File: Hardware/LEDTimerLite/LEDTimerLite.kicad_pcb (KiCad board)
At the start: 4 copper layers, 37.3 x 23.1 mm, 27 parts, among them J1 Program, J2 LED, J3 PWR, Q1 S8050, SW1 SW_Push, SW4 SW_PWR, U1 AP7383-36WW7, U2 PIC16LF18326, U4 BCR_421U_E6327, Y1 32.768 kHz

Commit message: LTL: try new PCB layout
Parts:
- added D2: Red LED, LED_SMD:LED_0805_2012Metric_Pad1.15x1.40mm_HandSolder, F.Cu at (138.8, 64.8)
- added R4: 560, Resistor_SMD:R_0805_2012Metric_Pad1.20x1.40mm_HandSolder, F.Cu at (134.0, 69.8)
- C1, C2, D1, Q1, R1, R2, R3, R5, U1, U4: moved to F.Cu
- J2, J3: moved to B.Cu
- moved H1 51.0 mm to (93.1, 70.4)
- moved H4 31.1 mm to (137.5, 70.4)
- moved J1 30.8 mm to (122.1, 58.3)
- moved H3 29.4 mm to (137.5, 59.2)
- moved J3 27.6 mm to (101.1, 63.5)
- moved R3 26.7 mm to (108.7, 69.5), turned to 90 degrees
- moved SW4 26.2 mm to (100.0, 70.5)
- moved C1 25.1 mm to (99.2, 64.8), turned to 90 degrees
- moved U1 25.1 mm to (96.0, 64.8)
- moved D1 22.1 mm to (104.4, 64.4), turned to 180 degrees
- moved H2 21.8 mm to (93.1, 59.2)
- moved Q1 21.5 mm to (105.1, 61.0)
- moved R1 20.7 mm to (101.1, 61.3)
- moved R2 20.7 mm to (101.1, 59.3)
- moved CG1 19.4 mm to (118.6, 63.0), turned to 90 degrees
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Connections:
- U2 pad 8: unconnected-(U2-RC1-Pad8) -> /LED
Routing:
- net /LED_EN_PWM: track 24.5 -> 0.00 mm, vias 3 -> 0
- net +5V: track 24.5 -> 0.00 mm
- net Net-(U2-RC0): track 18.3 -> 0.00 mm
- net /~{MCLR}/VPP: track 17.6 -> 0.00 mm, vias 1 -> 0
- net /ICSPCLK_RXD: track 15.5 -> 0.00 mm, vias 1 -> 0
- net Net-(U1-VOUT): track 13.3 -> 0.00 mm, vias 2 -> 0
- net /ICSPDAT_TXD: track 12.9 -> 0.00 mm, vias 1 -> 0
- net Net-(U4-Rext): track 12.1 -> 0.00 mm, vias 1 -> 0
- net /LDO_SENSE: track 10.4 -> 0.00 mm, vias 1 -> 0
- net Net-(SW4-C): track 10.2 -> 0.00 mm
- net Net-(J2-Pin_2): track 8.03 -> 0.00 mm
- net Net-(U2-RA5): track 6.34 -> 0.00 mm
- net Net-(CD1-Pad1): track 4.94 -> 0.00 mm
- net Net-(Q1-B): track 4.82 -> 0.00 mm
- net Net-(U2-RA4): track 4.55 -> 0.00 mm
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- removed copper zone on In2.Cu, net +3V3
- removed copper zone on In1.Cu, net GND
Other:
- board size 37.3 x 23.1 mm -> 49.5 x 16.3 mm

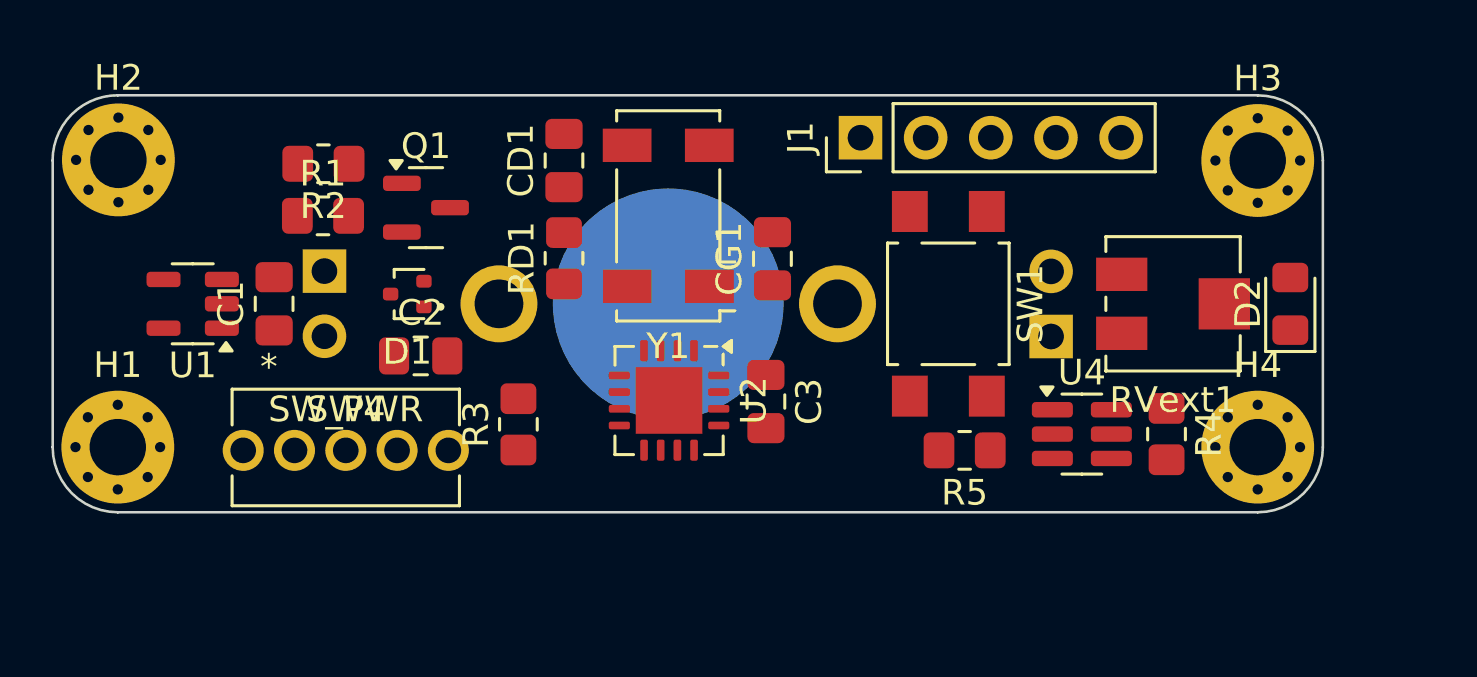
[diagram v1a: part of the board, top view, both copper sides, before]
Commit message: LTL: improve track routing
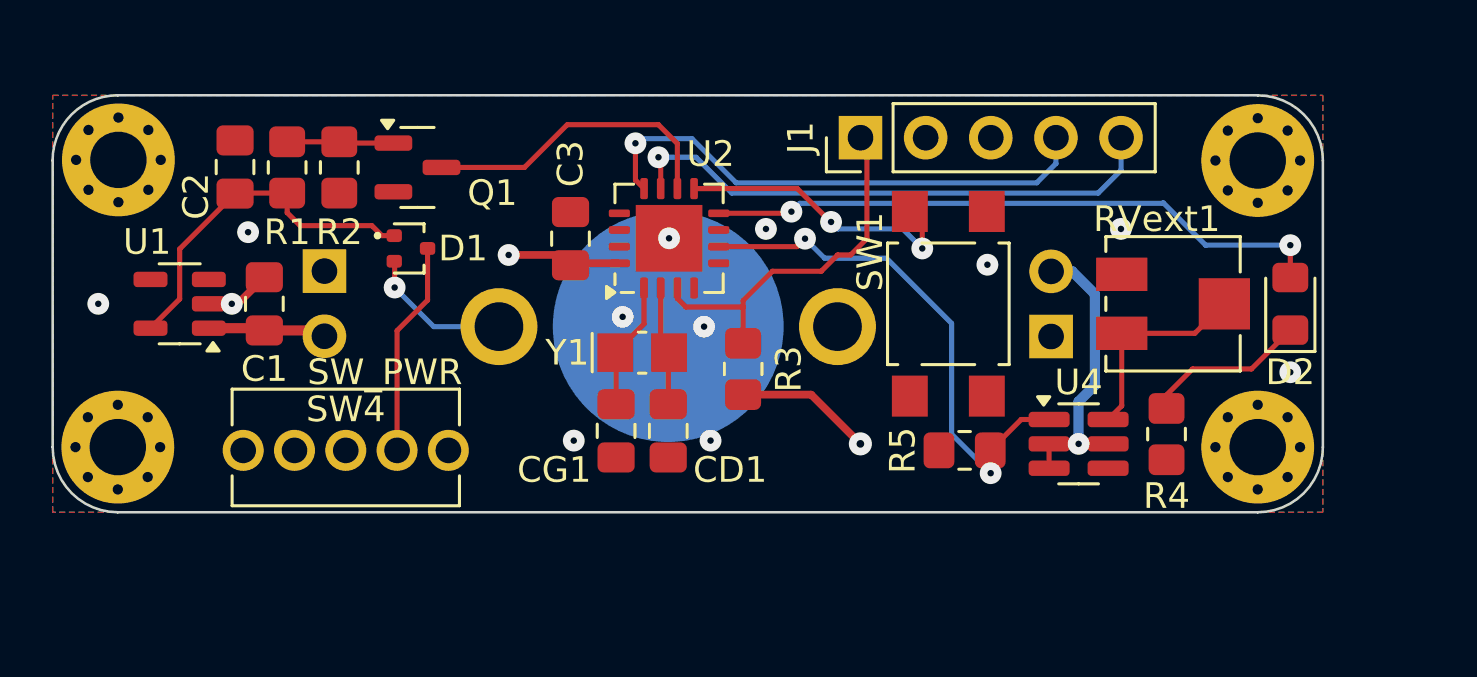
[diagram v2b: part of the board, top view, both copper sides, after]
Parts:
- removed RD1: 220k, Resistor_SMD:R_0805_2012Metric_Pad1.20x1.40mm_HandSolder
- Y1: footprint Crystal:Crystal_SMD_Abracon_ABS25-4Pin_8.0x3.8mm -> Crystal:Crystal_SMD_MicroCrystal_CC8V-T1A-2Pin_2.0x1.2mm_HandSoldering
- moved CD1 11.3 mm to (114.6, 69.7), turned to -90 degrees
- moved C2 10.3 mm to (97.7, 59.4), turned to 90 degrees
- moved C3 9.92 mm to (110.7, 62.2), turned to 90 degrees
- moved CG1 9.07 mm to (112.5, 69.7), turned to -90 degrees
- moved R3 9.03 mm to (117.5, 67.3)
- moved U2 6.32 mm to (114.6, 62.2), turned to 90 degrees
- moved Y1 5.43 mm to (113.5, 66.7), turned to 0 degrees
- moved R1 2.35 mm to (99.7, 59.5), turned to 90 degrees
- moved D1 1.78 mm to (104.5, 62.6), turned to 0 degrees
- moved Q1 1.60 mm to (104.8, 59.5)
- moved BT1 0.89 mm to (114.6, 65.7)
- moved R2 0.64 mm to (101.7, 59.5), turned to -90 degrees
- moved U1 0.51 mm to (95.5, 64.8)
- moved U4 0.40 mm to (130.6, 70.2)
- moved C1 0.38 mm to (98.8, 64.8)
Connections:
- CD1 pad 1: Net-(CD1-Pad1) -> Net-(U2-RA4)
- Y1 pad 2: GND -> Net-(U2-RA4)
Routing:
- net +5V: track 0.00 -> 35.6 mm
- net /LED: track 0.00 -> 24.4 mm, vias 0 -> 2
- net /ICSPCLK_RXD: track 0.00 -> 21.5 mm, vias 0 -> 1
- net /LED_EN_PWM: track 0.00 -> 20.7 mm, vias 0 -> 2
- net /ICSPDAT_TXD: track 0.00 -> 20.4 mm, vias 0 -> 1
- net /~{MCLR}/VPP: track 0.00 -> 14.6 mm
- net Net-(U1-VOUT): track 0.00 -> 14.0 mm
- net /LDO_SENSE: track 0.00 -> 11.9 mm
- net Net-(U2-RC0): track 0.00 -> 11.5 mm, vias 0 -> 2
- net Net-(J2-Pin_2): track 0.00 -> 11.4 mm, vias 0 -> 1
- net +3V3: track 0.00 -> 9.88 mm, vias 0 -> 2
- net Net-(SW4-C): track 0.00 -> 8.37 mm
- net Net-(U4-Rext): track 0.00 -> 8.06 mm
- net Net-(D2-K): track 0.00 -> 6.40 mm
- net Net-(BT1-+): track 0.00 -> 5.73 mm, vias 0 -> 1
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- added copper zone on In2.Cu, net +3V3
- added copper zone on B.Cu, net GND
- added copper zone on F.Cu, net GND
- added copper zone on In1.Cu, net GND

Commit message: LTL: improve track routing
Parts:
- SW4: value SW_PWR -> PWR
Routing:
- net GND: track 1.70 -> 8.03 mm, vias 12 -> 13
- net Net-(U2-RC0): track 11.5 -> 13.2 mm
- net Net-(J2-Pin_2): track 11.4 -> 12.2 mm
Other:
- board text added: "CR1220"
- board text added: "GND"
- board text added: "Input"
- board text added: "LED Timer Lite v1.0 GH: tomikaa87"
- board text added: "MCLR"
- board text added: "OFF"
- board text added: "ON"
- board text added: "Output"
- board text added: "PGM"
- board text added: "RX"
- board text added: "TX"
- board text added: "VCC"
- board text removed: "LED Timer V1"
- board text removed: "github: tomikaa87"

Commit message: LTL: replace BAT54C with 1SS384 (lower Vf)
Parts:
- D1: value BAT54C -> Red LED; footprint Package_TO_SOT_SMD:SOT-416 -> LED_SMD:LED_0805_2012Metric_Pad1.15x1.40mm_HandSolder
- D2: value Red LED -> 1SS384; footprint LED_SMD:LED_0805_2012Metric_Pad1.15x1.40mm_HandSolder -> Package_TO_SOT_SMD:SOT-343_SC-70-4
- SW4: value PWR -> SW_PWR
- moved D1 34.4 mm to (138.8, 64.8), turned to 90 degrees
- moved D2 34.3 mm to (104.5, 63.0), turned to -90 degrees
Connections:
- C2 pad 1: Net-(U1-VOUT) -> Net-(D2B-A)
- D1 pad 1: Net-(U1-VOUT) -> Net-(D1-K)
- D1 pad 2: Net-(BT1-+) -> /LED
- D2 pad 1: Net-(D2-K) -> Net-(BT1-+)
- D2 pad 2: /LED -> Net-(D2B-A)
- R1 pad 1: Net-(U1-VOUT) -> Net-(D2B-A)
- R4 pad 1: Net-(D2-K) -> Net-(D1-K)
- SW4 pad 3: Net-(SW4-C) -> Net-(D2A-K)
- U1 pad 5: Net-(U1-VOUT) -> Net-(D2B-A)
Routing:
- net Net-(U1-VOUT): track 14.0 -> 0.00 mm
- net Net-(D2B-A): track 0.00 -> 13.9 mm
- net Net-(SW4-C): track 8.37 -> 0.00 mm
- net Net-(D2A-K): track 0.00 -> 8.22 mm
- net Net-(D2-K): track 6.40 -> 0.00 mm
- net Net-(D1-K): track 0.00 -> 6.40 mm
- net Net-(BT1-+): track 5.73 -> 5.10 mm, vias 1 -> 0
